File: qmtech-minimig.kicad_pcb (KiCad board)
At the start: 4 copper layers, 142.2 x 92 mm, 150 parts, among them IC1 RTL8211EG-VB-CG, J1 DB9_Male, J2 DB9_Male, J3 SCHA5B0200, J4 ARM_JTAG, J5 AUDIO-CONNECTOR-6P-SMD-344003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, J6 Mini-DIN-6, J8 HR911130A, J9 47151-0001, SW1 SW_Push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

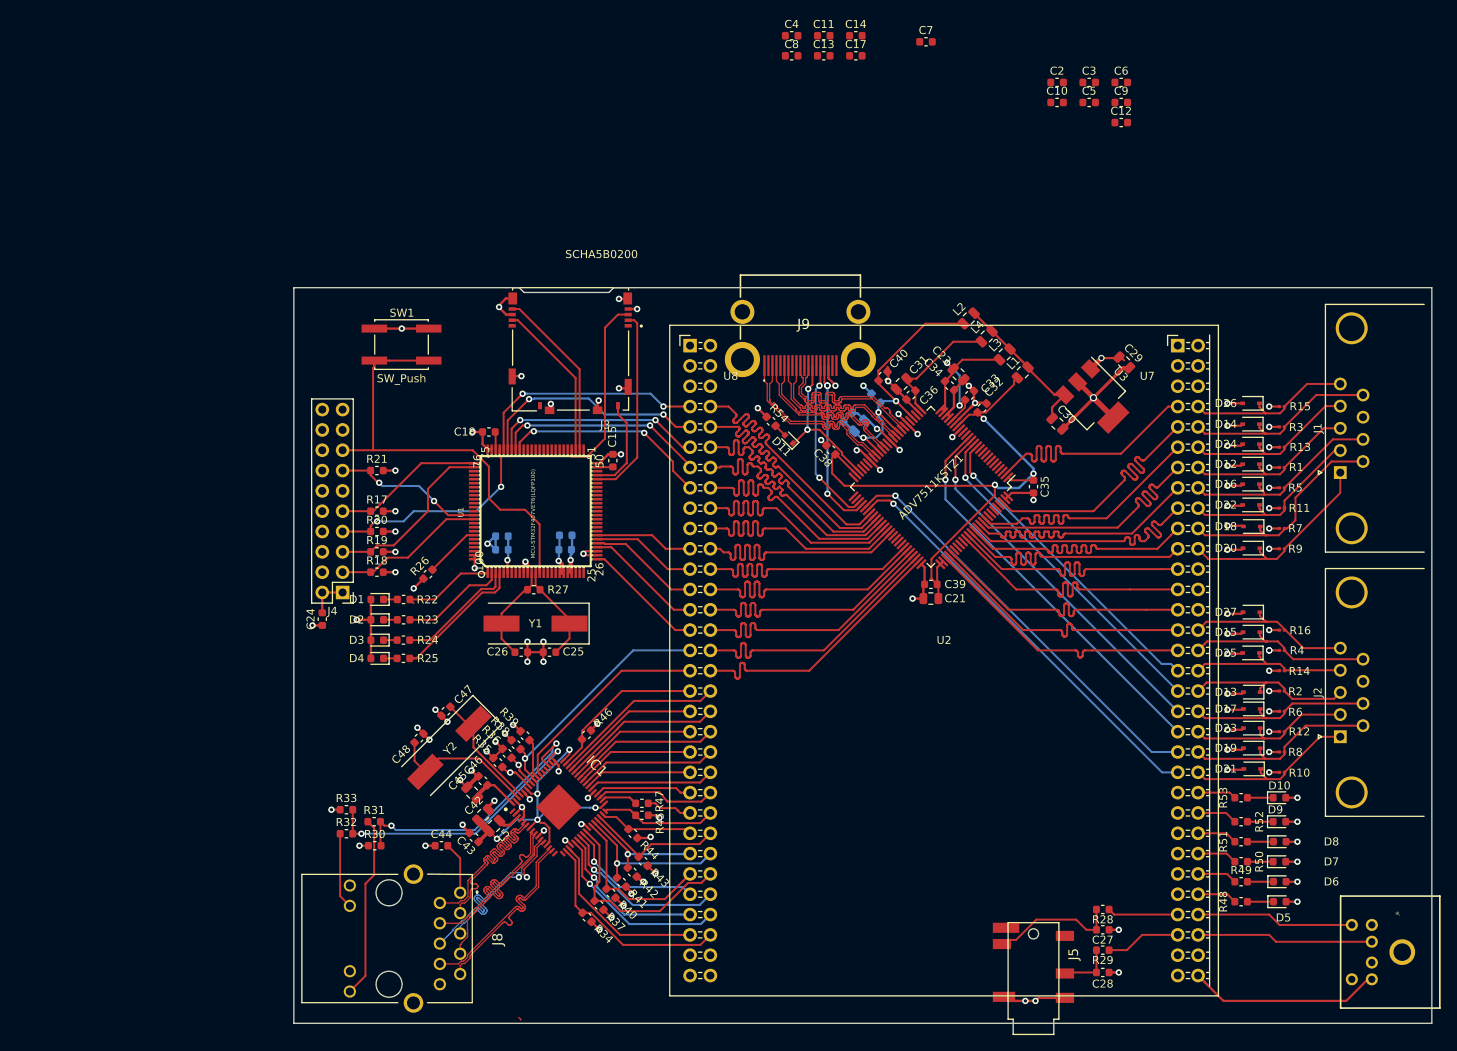
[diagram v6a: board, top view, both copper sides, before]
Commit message: Fixed connections for the adv7511. Fixed some minor footprint issues with the fpga board footprint.
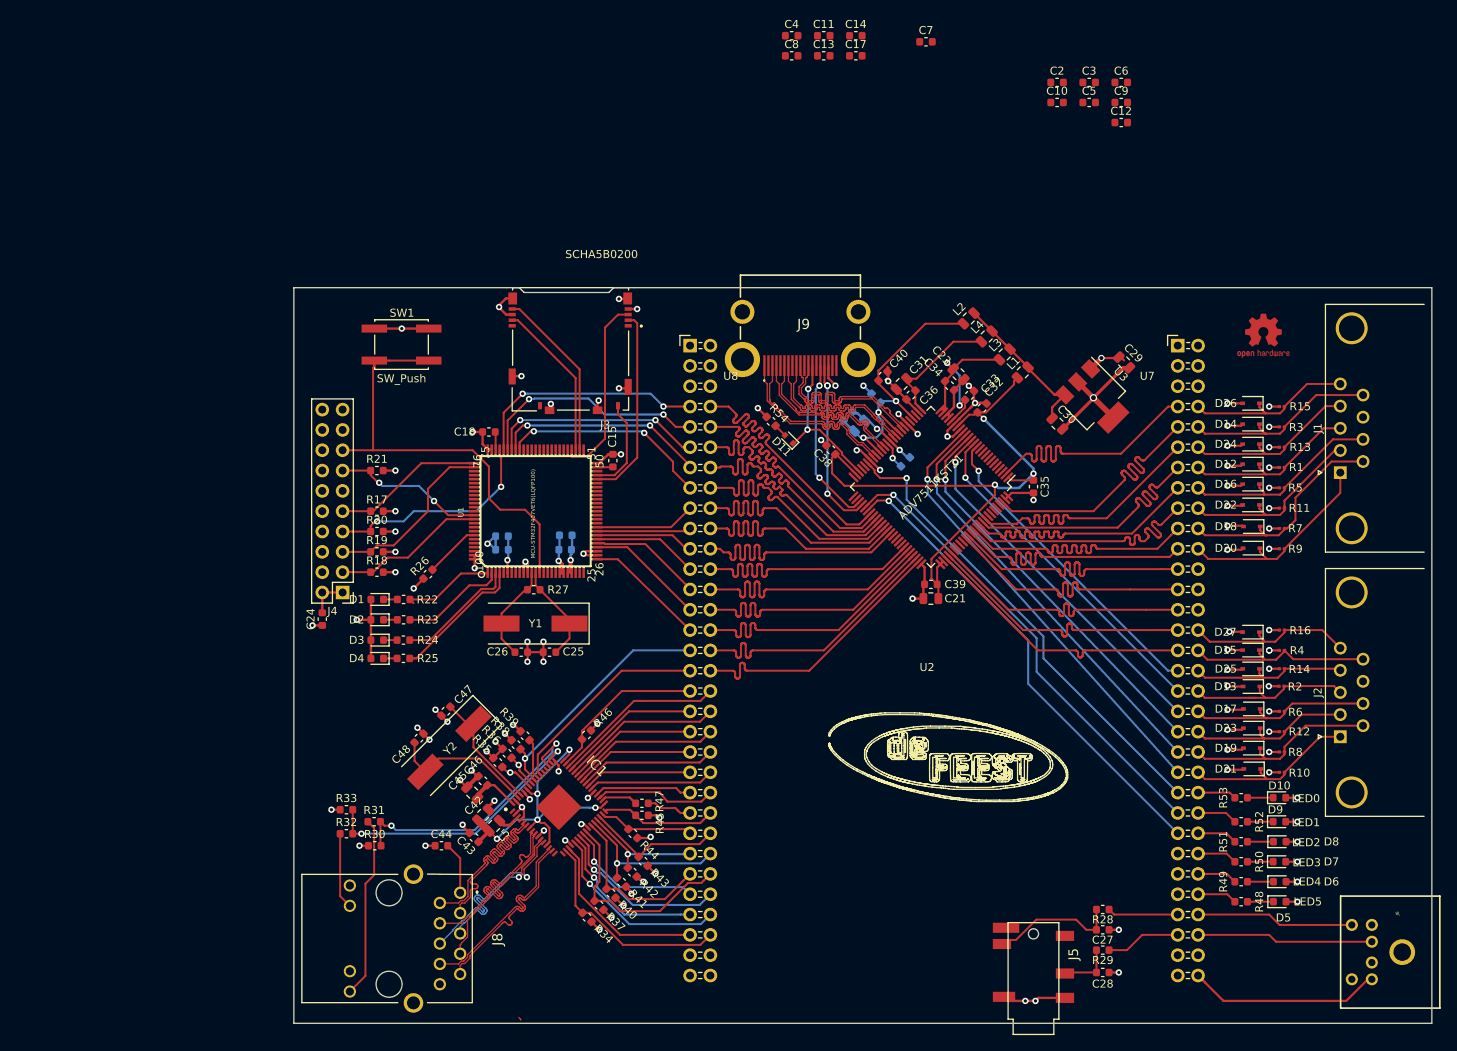
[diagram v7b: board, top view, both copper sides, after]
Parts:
- added R55: 2K, Resistor_SMD:R_0603_1608Metric, B.Cu at (127.2, 85.0)
- added REF**: OSHW-Logo2_7.3x6mm_Copper, Symbol:OSHW-Logo2_7.3x6mm_Copper, F.Cu at (172.0, 69.2)
- moved D27 2.50 mm to (170.4, 106.3)
- moved D15 2.25 mm to (170.4, 108.5)
- moved D25 2.00 mm to (170.4, 110.9)
- moved D13 0.70 mm to (170.5, 113.1)
- moved R2 0.60 mm to (174.3, 113.1)
- moved R14 0.25 mm to (174.3, 110.9)
- moved C37 0.15 mm to (120.1, 79.3)
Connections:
- ADV7511KSTZ1 pad 45: Net-(ADV7511KSTZ1-Pad45) -> ADV_INT
- U1 pad 33: Net-(U1-Pad33) -> STM_IO_33
- U1 pad 34: Net-(U1-Pad34) -> STM_IO_34
- U2 pad U717: Net-(U2-PadU717) -> STM_IO_34
- U2 pad U719: Net-(U2-PadU719) -> STM_IO_33
- U2 pad U841: ADV_SCL -> ADV_SCLK
- U2 pad U843: ADV_SDA -> ADV_LRCLK
- U2 pad U845: Net-(U2-PadU845) -> ADV_INT
- U2 pad U847: Net-(U2-PadU847) -> ADV_SCL
- U2 pad U849: Net-(U2-PadU849) -> ADV_SDA
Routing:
- net ADV_INT: track 0.00 -> 59.2 mm, vias 0 -> 1
- net ADV_LRCLK: track 0.00 -> 56.3 mm, vias 0 -> 1
- net ADV_SCLK: track 0.00 -> 53.0 mm, vias 0 -> 1
- net STM_IO_34: track 0.00 -> 12.5 mm
- net STM_IO_33: track 0.00 -> 11.7 mm
- net ADV_SDA: track 53.3 -> 59.7 mm
- net ADV_SCL: track 53.0 -> 58.7 mm
- net GND: track 197.8 -> 201.6 mm
- net Net-(ADV7511KSTZ1-Pad38): track 0.00 -> 3.72 mm, vias 0 -> 1
- net JS2_3: track 21.2 -> 21.7 mm

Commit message: Connected adv7511 unused inputs to ground. Added high voltage protection on PS2 port. Added indicators for the rubber glue on feet.
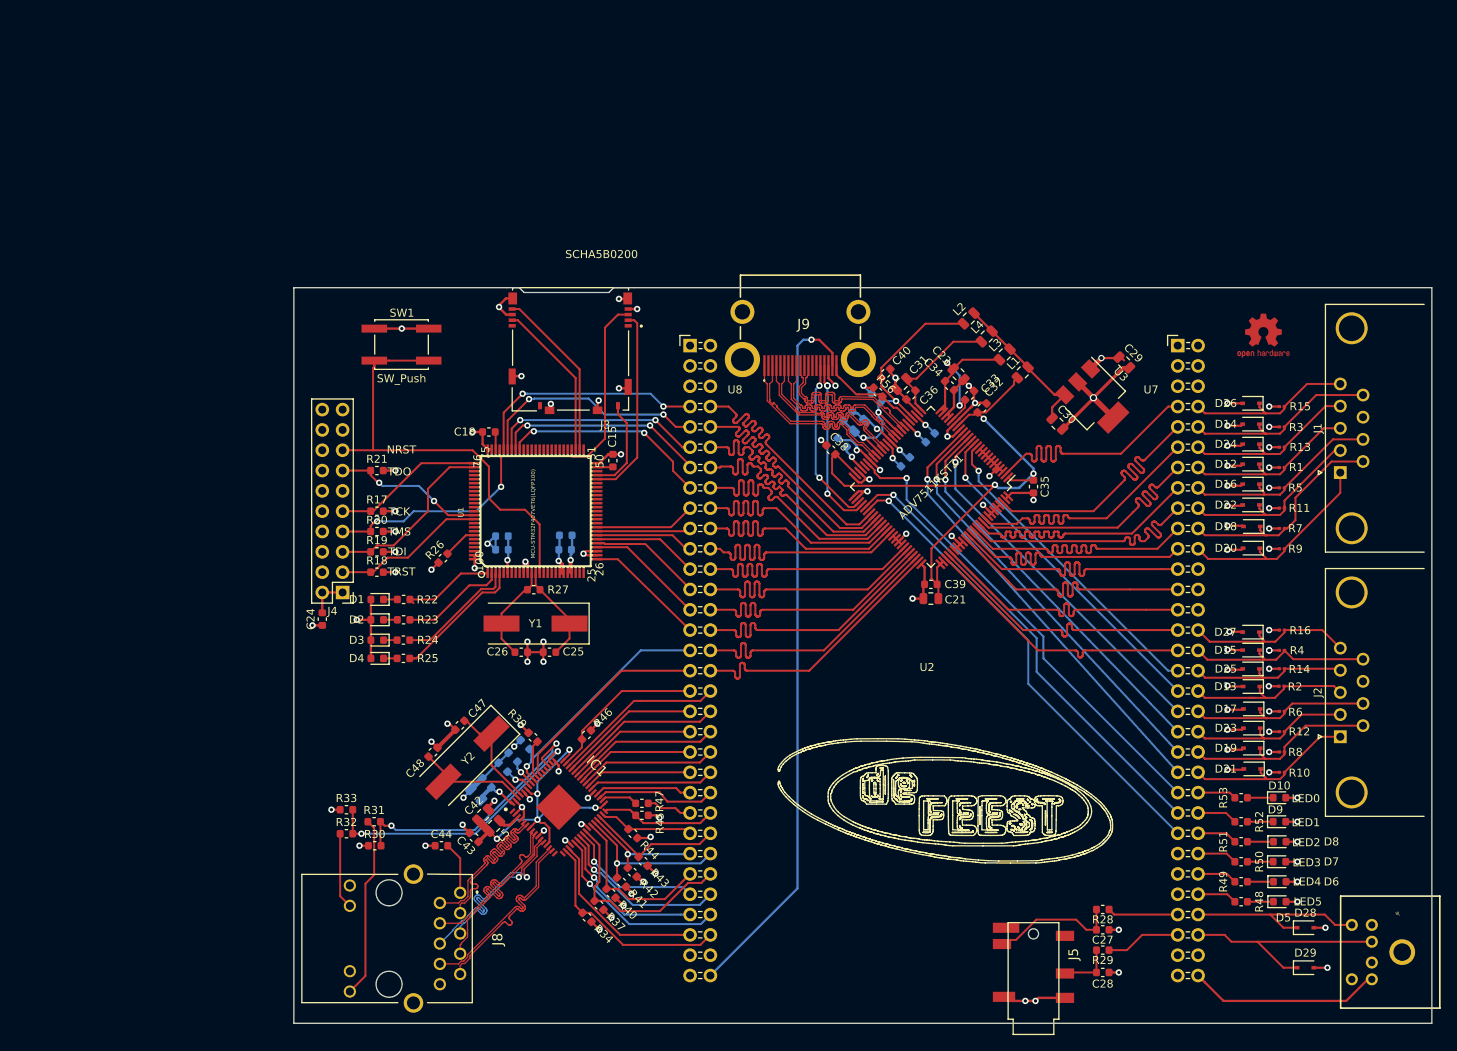
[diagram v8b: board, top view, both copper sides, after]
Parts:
- removed C10, C11, C12, C13, C17, C2, C3, C4, C5, C6, C7, C8, C9: 100nF, Capacitor_SMD:C_0603_1608Metric
- removed D11: D, Diode_SMD:D_SOD-523
- removed R54: 27K, Resistor_SMD:R_0603_1608Metric
- added D28: 3.6V, Diode_SMD:D_SOD-323, F.Cu at (177.2, 143.2)
- added D29: 3.6V, Diode_SMD:D_SOD-323, F.Cu at (177.2, 148.2)
- added R56: 10k, Resistor_SMD:R_0603_1608Metric, F.Cu at (123.8, 76.3)
- added R57: 887, Resistor_SMD:R_0603_1608Metric, B.Cu at (130.3, 82.0)
- C14, C45, C46, R35, R36, R38: moved to B.Cu
- moved C14 73.8 mm to (84.7, 96.0), turned to 180 degrees
- moved C1 37.1 mm to (119.3, 82.6), turned to 315 degrees
- moved R26 2.75 mm to (69.4, 97.1)
- moved Y2 2.58 mm to (72.5, 122.0)
- moved C47 2.47 mm to (71.6, 117.9)
- moved C48 2.47 mm to (68.2, 121.3)
- moved R38 1.13 mm to (79.7, 120.4)
- moved R39 1.01 mm to (80.7, 119.4)
- moved R36 0.89 mm to (78.2, 121.9)
- moved R35 0.87 mm to (76.9, 123.2)
- moved C45 0.56 mm to (73.6, 126.6)
- moved C46 0.56 mm to (74.9, 125.1)
- moved C40 0.49 mm to (124.8, 74.0)
- turned C38 to 315 degrees
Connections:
- ADV7511KSTZ1 pad 10: Net-(ADV7511KSTZ1-Pad10) -> GND
- ADV7511KSTZ1 pad 11: Net-(ADV7511KSTZ1-Pad11) -> GND
- ADV7511KSTZ1 pad 3: Net-(ADV7511KSTZ1-Pad3) -> GND
- ADV7511KSTZ1 pad 30: Net-(ADV7511KSTZ1-Pad30) -> ADV_HPD
- ADV7511KSTZ1 pad 4: Net-(ADV7511KSTZ1-Pad4) -> GND
- ADV7511KSTZ1 pad 47: Net-(ADV7511KSTZ1-Pad47) -> 3V3
- ADV7511KSTZ1 pad 48: ADV_CEC -> GND
- ADV7511KSTZ1 pad 5: Net-(ADV7511KSTZ1-Pad5) -> GND
- ADV7511KSTZ1 pad 50: ADV_CEC_CLK -> GND
- ADV7511KSTZ1 pad 51: ADV_HEAC- -> GND
- ADV7511KSTZ1 pad 52: ADV_HEAC+ -> GND
- ADV7511KSTZ1 pad 6: Net-(ADV7511KSTZ1-Pad6) -> GND
- ADV7511KSTZ1 pad 65: Net-(ADV7511KSTZ1-Pad65) -> GND
- ADV7511KSTZ1 pad 66: Net-(ADV7511KSTZ1-Pad66) -> GND
- ADV7511KSTZ1 pad 67: Net-(ADV7511KSTZ1-Pad67) -> GND
- ADV7511KSTZ1 pad 68: Net-(ADV7511KSTZ1-Pad68) -> GND
- ADV7511KSTZ1 pad 7: Net-(ADV7511KSTZ1-Pad7) -> GND
- ADV7511KSTZ1 pad 8: Net-(ADV7511KSTZ1-Pad8) -> GND
- ADV7511KSTZ1 pad 81: Net-(ADV7511KSTZ1-Pad81) -> GND
- ADV7511KSTZ1 pad 82: Net-(ADV7511KSTZ1-Pad82) -> GND
- ADV7511KSTZ1 pad 83: Net-(ADV7511KSTZ1-Pad83) -> GND
- ADV7511KSTZ1 pad 84: Net-(ADV7511KSTZ1-Pad84) -> GND
- ADV7511KSTZ1 pad 9: Net-(ADV7511KSTZ1-Pad9) -> GND
- ADV7511KSTZ1 pad 93: Net-(ADV7511KSTZ1-Pad93) -> GND
- ADV7511KSTZ1 pad 94: Net-(ADV7511KSTZ1-Pad94) -> GND
- ADV7511KSTZ1 pad 95: Net-(ADV7511KSTZ1-Pad95) -> GND
- ADV7511KSTZ1 pad 96: Net-(ADV7511KSTZ1-Pad96) -> GND
- ADV7511KSTZ1 pad 97: Net-(ADV7511KSTZ1-Pad97) -> GND
- C38 pad 1: ADV_DVDD -> GND
- C38 pad 2: GND -> ADV_DVDD
- J9 pad 18: ADV_5V -> VIN5V
- J9 pad 19: ADV_HOTPLUG -> ADV_HPD
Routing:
- net VIN5V: track 24.2 -> 114.3 mm, vias 0 -> 1
- net GND: track 201.6 -> 231.7 mm, vias 74 -> 76
- net ADV_CEC: track 19.5 -> 0.00 mm, vias 2 -> 0
- net ADV_HPD: track 0.00 -> 12.7 mm
- net PS2_DAT1: track 22.1 -> 28.4 mm
- net ETH_CKXTAL2: track 18.5 -> 14.1 mm
- net PS2_CLK1: track 19.8 -> 23.8 mm
- net Net-(ADV7511KSTZ1-Pad28): track 0.00 -> 3.32 mm, vias 0 -> 1
- net Net-(R26-Pad2): track 6.95 -> 4.23 mm
- net ETH_CKXTAL1: track 15.1 -> 13.0 mm
- net Net-(D11-Pad2): track 1.68 -> 0.00 mm
- net 3V3: track 92.1 -> 93.1 mm, vias 47 -> 48
- net Net-(IC1-Pad58): track 4.39 -> 3.50 mm
- net ETH_INTB: track 30.9 -> 30.1 mm
- net Net-(IC1-Pad57): track 4.29 -> 3.48 mm
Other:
- board text added: "NRST"
- board text added: "Paul Honig (paul@scene.rs) deFEEST retro entertainment 2019 Version: 0.500 CERN Open Hardware Licence"
- board text added: "TCK"
- board text added: "TDI"
- board text added: "TDO"
- board text added: "TMS"
- board text added: "TRST"
